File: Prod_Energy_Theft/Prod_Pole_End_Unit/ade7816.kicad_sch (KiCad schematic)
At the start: 56 parts, among them J17 Screw_Terminal_01x02, J18 Screw_Terminal_01x02, J19 Screw_Terminal_01x02, J20 Screw_Terminal_01x02, J21 Screw_Terminal_01x02, J22 Screw_Terminal_01x02, J24 Screw_Terminal_01x01, J25 Screw_Terminal_01x01, U19 ADE7816ACPZ, Y3 Crystal

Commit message: Chnages in power and ADE7816
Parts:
- removed C74, C75: 22nf, Capacitor_SMD:C_0805_2012Metric, symbol Device:C
- removed J24, J25: Screw_Terminal_01x01, custom:TerminalBlock_1x01_P5.08mm, symbol Connector:Screw_Terminal_01x01
- removed R84, R85: 10k, Resistor_SMD:R_0805_2012Metric, symbol Device:R
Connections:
- net GND: now also J17.2 (Pin_2), J18.2 (Pin_2), J19.2 (Pin_2), J20.2 (Pin_2), J21.2 (Pin_2), J22.2 (Pin_2), R65.2, R66.2, R67.2, R68.2, R69.2, R71.1, R73.1, R75.1, R77.1, R79.1, R83.2, R86.1
- no-connect marks 4 -> 6

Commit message: PCB
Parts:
- J17, J18, J19, J20, J21, J22: footprint TerminalBlock_Phoenix:TerminalBlock_Phoenix_PTSM-0,5-2-2,5-V-SMD_1x02-1MP_P2.50mm_Vertical -> TerminalBlock_Phoenix:TerminalBlock_Phoenix_MKDS-1,5-2-5.08_1x02_P5.08mm_Horizontal
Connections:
- net +3.3V: no longer R97.2, U19.2 (PULL_HIGH)
- net +3.3V_ADE: now also R97.2, U19.2 (PULL_HIGH)
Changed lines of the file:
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@@
 			)
 		)
-		(property "Footprint" "TerminalBlock_Phoenix:TerminalBlock_Phoenix_PTSM-0,5-2-2,5-V-SMD_1x02-1MP_P2.50mm_Vertical"
+		(property "Footprint" "TerminalBlock_Phoenix:TerminalBlock_Phoenix_MKDS-1,5-2-5.08_1x02_P5.08mm_Horizontal"
 			(at 29.21 105.41 0)
 			(effects
@@
 			)
 		)
-		(property "Footprint" "TerminalBlock_Phoenix:TerminalBlock_Phoenix_PTSM-0,5-2-2,5-V-SMD_1x02-1MP_P2.50mm_Vertical"
+		(property "Footprint" "TerminalBlock_Phoenix:TerminalBlock_Phoenix_MKDS-1,5-2-5.08_1x02_P5.08mm_Horizontal"
 			(at 29.21 168.91 0)
 			(effects
@@
 			)
 		)
-		(property "Footprint" "TerminalBlock_Phoenix:TerminalBlock_Phoenix_PTSM-0,5-2-2,5-V-SMD_1x02-1MP_P2.50mm_Vertical"
+		(property "Footprint" "TerminalBlock_Phoenix:TerminalBlock_Phoenix_MKDS-1,5-2-5.08_1x02_P5.08mm_Horizontal"
 			(at 101.6 168.91 0)
 			(effects
@@
 			)
 		)
-		(property "Value" "+3.3V"
+		(property "Value" "+3.3V_ADE"
 			(at 168.402 119.634 0)
 			(effects
@@
 			)
 		)
-		(property "Footprint" "TerminalBlock_Phoenix:TerminalBlock_Phoenix_PTSM-0,5-2-2,5-V-SMD_1x02-1MP_P2.50mm_Vertical"
+		(property "Footprint" "TerminalBlock_Phoenix:TerminalBlock_Phoenix_MKDS-1,5-2-5.08_1x02_P5.08mm_Horizontal"
 			(at 29.21 29.21 0)
 			(effects
@@
 			)
 		)
-		(property "Value" "+3.3V"
+		(property "Value" "+3.3V_ADE"
 			(at 256.54 113.0299 90)
 			(effects
@@
 			)
 		)
-		(property "Footprint" "TerminalBlock_Phoenix:TerminalBlock_Phoenix_PTSM-0,5-2-2,5-V-SMD_1x02-1MP_P2.50mm_Vertical"
+		(property "Footprint" "TerminalBlock_Phoenix:TerminalBlock_Phoenix_MKDS-1,5-2-5.08_1x02_P5.08mm_Horizontal"
 			(at 29.21 71.12 0)
 			(effects
@@
 			)
 		)
-		(property "Footprint" "TerminalBlock_Phoenix:TerminalBlock_Phoenix_PTSM-0,5-2-2,5-V-SMD_1x02-1MP_P2.50mm_Vertical"
+		(property "Footprint" "TerminalBlock_Phoenix:TerminalBlock_Phoenix_MKDS-1,5-2-5.08_1x02_P5.08mm_Horizontal"
 			(at 29.21 135.89 0)
 			(effects

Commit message: PCB Design
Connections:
- net +3.3V is gone; now on net +3.3V_ADE: R92.1
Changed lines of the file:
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@@
 			)
 		)
-		(property "Value" "+3.3V"
+		(property "Value" "+3.3V_ADE"
 			(at 168.91 71.12 0)
 			(effects

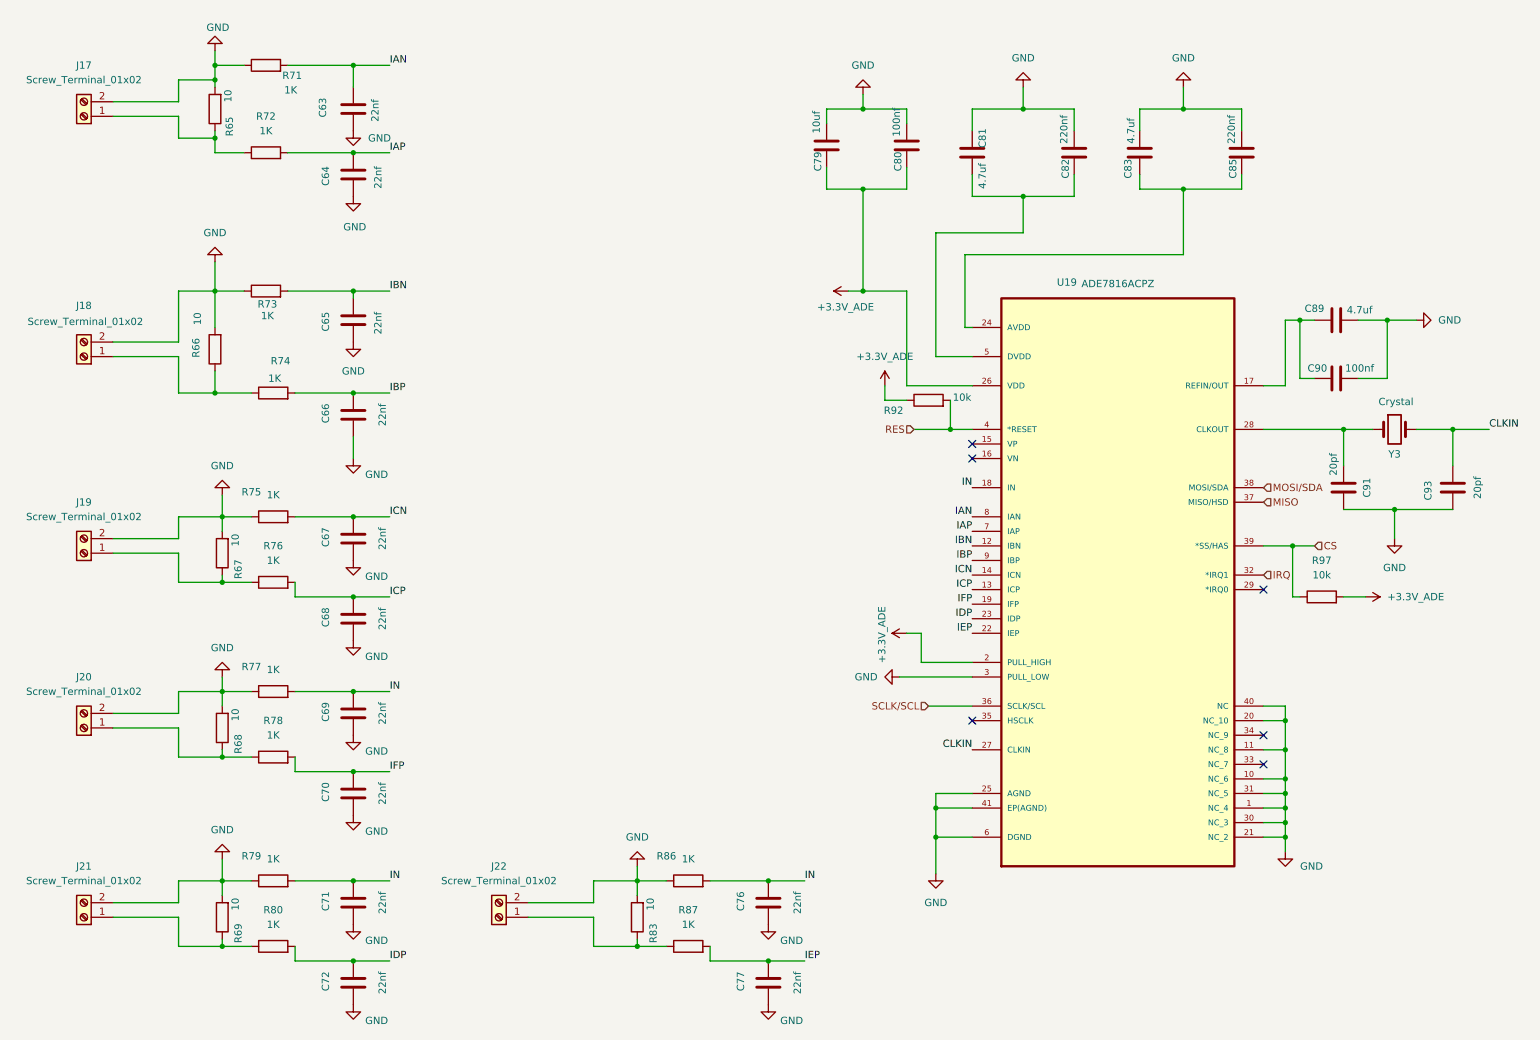
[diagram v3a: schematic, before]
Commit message: update in BOM list
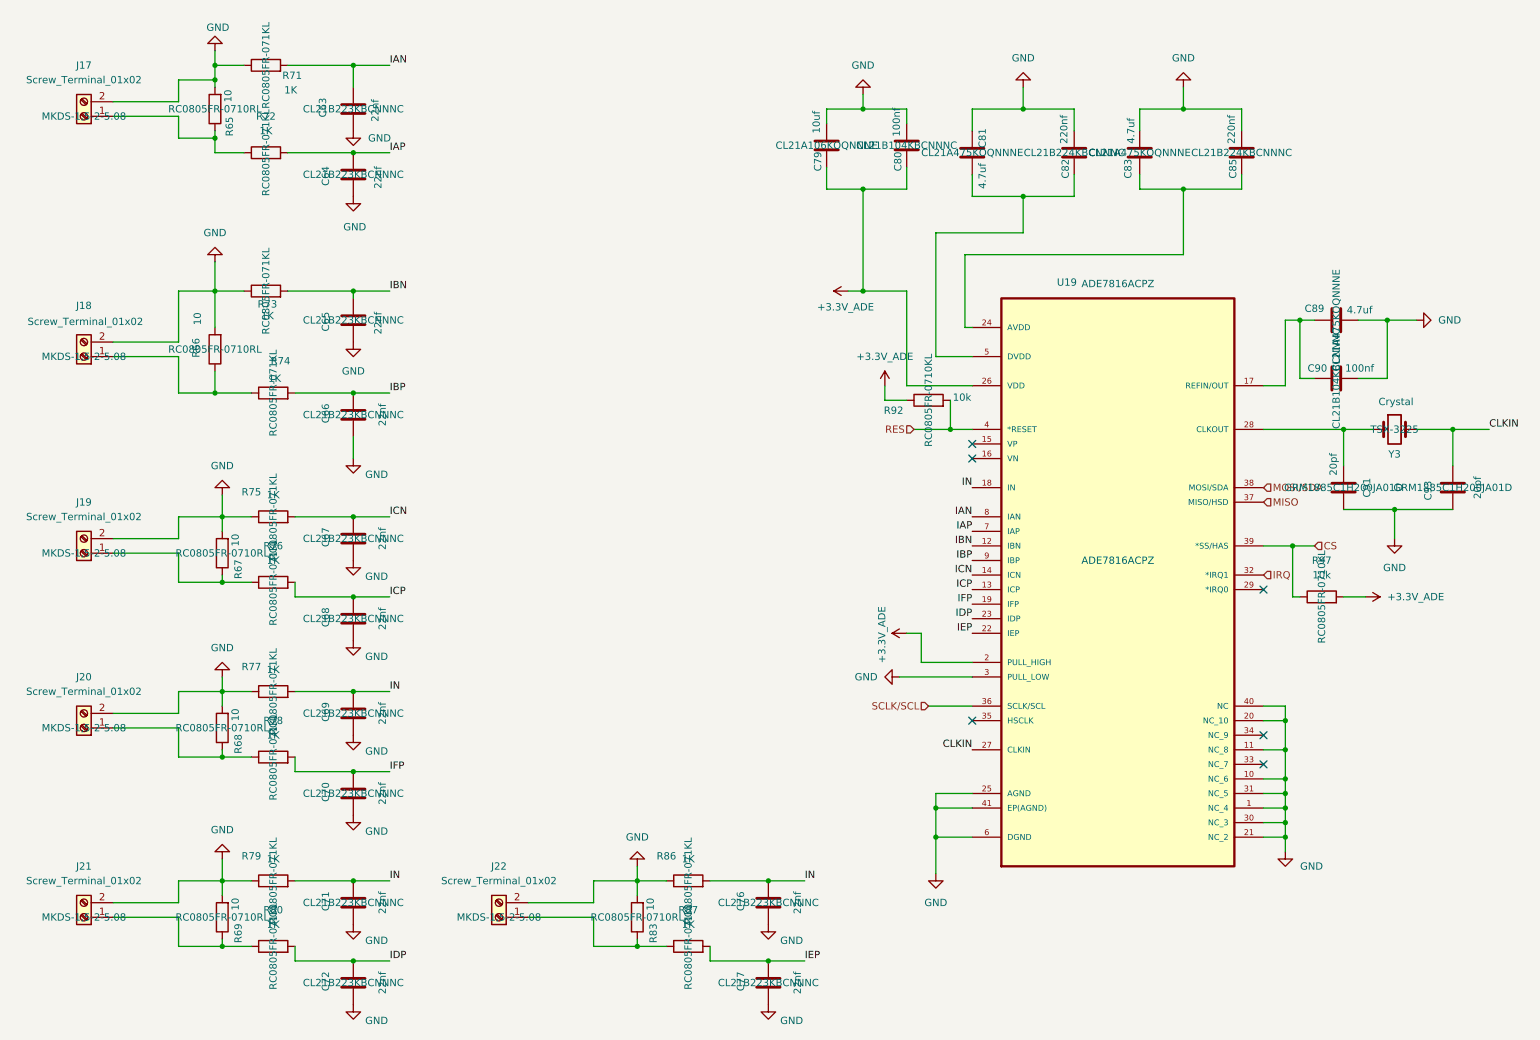
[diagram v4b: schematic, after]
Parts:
- C63, C64, C65, C66, C67, C68, C69, C70, C71, C72, C76, C77: Part Number (none) -> CL21B223KBCNNNC
- C79: Part Number (none) -> CL21A106KOQNNNE
- C80, C90: Part Number (none) -> CL21B104KBCNNNC
- C81, C83, C89: Part Number (none) -> CL21A475KOQNNNE
- C82, C85: Part Number (none) -> CL21B224KBCNNNC
- C91, C93: Part Number (none) -> GRM1885C1H200JA01D
- J17, J18, J19, J20, J21, J22: Part Number (none) -> MKDS-1,5-2-5.08
- R65, R66, R67, R68, R69, R83: Part Number (none) -> RC0805FR-0710RL
- R71, R72, R73, R74, R75, R76, R77, R78, R79, R80, R86, R87: Part Number (none) -> RC0805FR-071KL
- R92, R97: Part Number (none) -> RC0805FR-0710KL
- U19: Part Number (none) -> ADE7816ACPZ
- Y3: Part Number (none) -> TSX-3225
